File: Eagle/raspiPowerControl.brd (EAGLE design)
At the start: 100 x 80 mm, 14 parts, among them IC1 MCP1702/3 3.3, Q1 FDN360P, T1 BC847

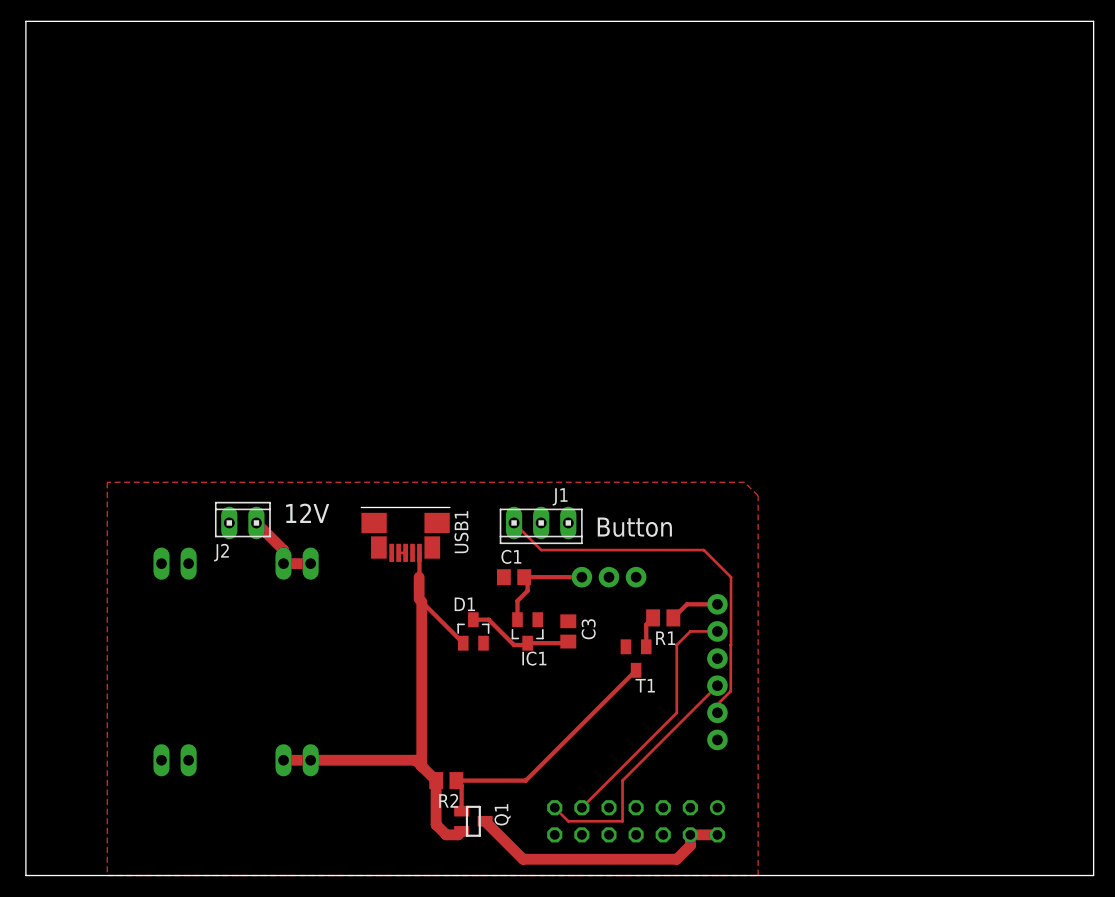
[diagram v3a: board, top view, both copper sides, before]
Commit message: Modified layout
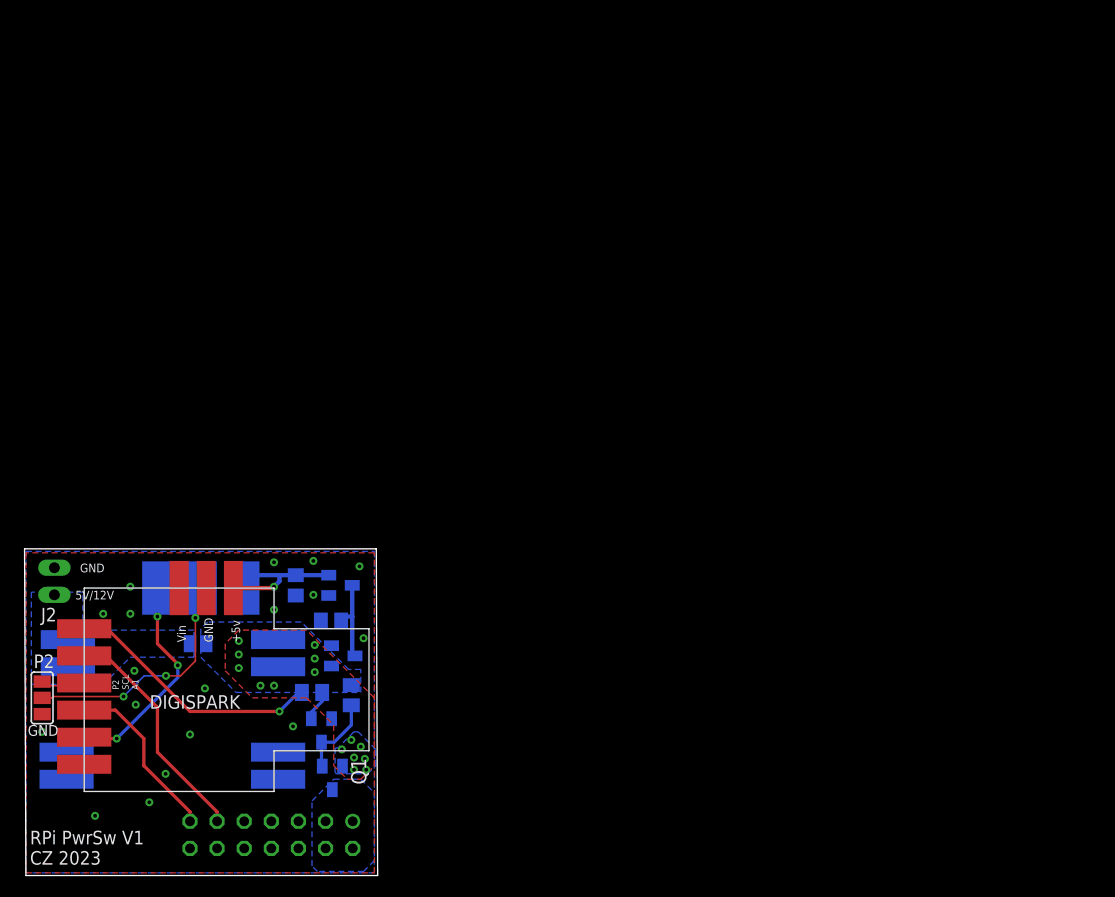
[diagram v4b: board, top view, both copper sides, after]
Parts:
- removed ATTINY85: DIGISPARK, raspiPowerControl:DIGISPARK
- removed J1: (no value), con-amp:10X03MTA
- removed USB1: MOLEX-47346-0001, usb_con-update:MOLEX-47364-0001
- added BUT: button, con-avx:009176003
- added DIGISPARK: DIGISPARKDIGISPARK-SMD, raspiPowerControl:DIGISPARK-SMD
- added P2: (no value), jumper:SJ_2
- added PWR=5V: (no value), jumper:SJ
- C3: value 100n -> 1u
- MP1584: value DCDC-MINI -> DCDC-MINIDCDC-MINI-SMD; device raspiPowerControl:DCDC-MINI -> raspiPowerControl:DCDC-MINI-SMD
- Q1: value FDN360P -> DMP3098
- moved SV1 34.2 mm to (23.0, 3.81)
- moved R1 33.6 mm to (26.8, 17.1), flipped to the bottom
- moved T1 30.2 mm to (27.7, 13.6), flipped to the bottom
- moved C3 22.2 mm to (28.6, 23.9), flipped to the bottom, turned to 180 degrees
- moved C1 20.5 mm to (25.3, 27.2), flipped to the bottom, turned to 90 degrees
- moved J2 18.5 mm to (2.67, 27.6), flipped to the bottom, turned to 90 degrees
- moved IC1 18.1 mm to (29.5, 27.2), flipped to the bottom, turned to 90 degrees
- moved Q1 13.8 mm to (28.7, 9.14), flipped to the bottom, turned to 180 degrees
- moved D1 12.4 mm to (29.7, 20.6), flipped to the bottom, turned to 90 degrees
- moved R2 12.0 mm to (30.5, 16.9), flipped to the bottom, turned to 90 degrees
- moved MP1584 8.56 mm to (13.5, 12.3), turned to 180 degrees
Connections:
- removed net +12V: J2.1, MP1584.3, MP1584.4
- removed net N$2: USB1.3, USB1.4
- removed net N$5: ATTINY85.P0, R1.1
- removed net N$6: ATTINY85.P4, J1.1
- new net 3V3: BUT.3, C1.2, DIGISPARK.5V, IC1.2
- new net BUT2: BUT.2, P2.2
- new net BUT4: BUT.1, DIGISPARK.P4
- new net P2: DIGISPARK.P2, P2.3
- new net SWPWR: DIGISPARK.P0, R1.1
- net +5V: now also MP1584.OUT+1, MP1584.OUT+2, PWR=5V.1; no longer MP1584.5, MP1584.6, USB1.1
- net GND: now also DIGISPARK.GND, J2.1, MP1584.IN-1, MP1584.IN-2, MP1584.OUT-1, MP1584.OUT-2, P2.1; no longer ATTINY85.GND, J1.2, J2.2, MP1584.1, MP1584.2, MP1584.7, MP1584.8, USB1.5
- net PWR: now also J2.2, MP1584.IN+1, MP1584.IN+2, PWR=5V.2; no longer ATTINY85.5V, C1.2, IC1.2, J1.3
- net RPDWN: now also DIGISPARK.P3; no longer ATTINY85.P3
- net SHUTDWN: now also DIGISPARK.P1; no longer ATTINY85.P1
- net VIN: now also DIGISPARK.VIN; no longer ATTINY85.VIN
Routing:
- net +5V: track 47.7 -> 0.00 mm, vias 0 -> 15
- net N$6: track 35.7 -> 0.00 mm
- net RP5V: track 24.8 -> 0.00 mm
- net SWPWR: track 0.00 -> 24.5 mm, vias 0 -> 1
- net BUT2: track 0.00 -> 22.9 mm, vias 0 -> 3
- net BUT4: track 0.00 -> 20.5 mm, vias 0 -> 3
- net N$3: track 24.2 -> 7.58 mm
- net 3V3: track 0.00 -> 14.1 mm, vias 0 -> 1
- net PWR: track 9.91 -> 0.00 mm
- net +12V: track 7.40 -> 0.00 mm
- net RPDWN: track 23.3 -> 16.2 mm
- net N$5: track 4.66 -> 0.00 mm
- net P2: track 0.00 -> 3.84 mm
- net N$1: track 10.0 -> 7.91 mm
- net SHUTDWN: track 23.3 -> 21.8 mm
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- added copper zone on layer 1, net +5V
- added copper zone on layer 16, net +5V
- added copper zone on layer 16, net GND
- added copper zone on layer 16, net PWR
- added copper zone on layer 16, net RP5V
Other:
- board size 100 x 80 mm -> 33.1 x 30.6 mm
- board text added: "3.3V"
- board text added: "5V/12V"
- board text added: "GND"
- board text added: "P2/GND"
- board text added: "P4"
- board text added: "Q1"
- board text added: "RPi PwrSw V1 CZ 2023"
- board text removed: "12V"
- board text removed: "Button"

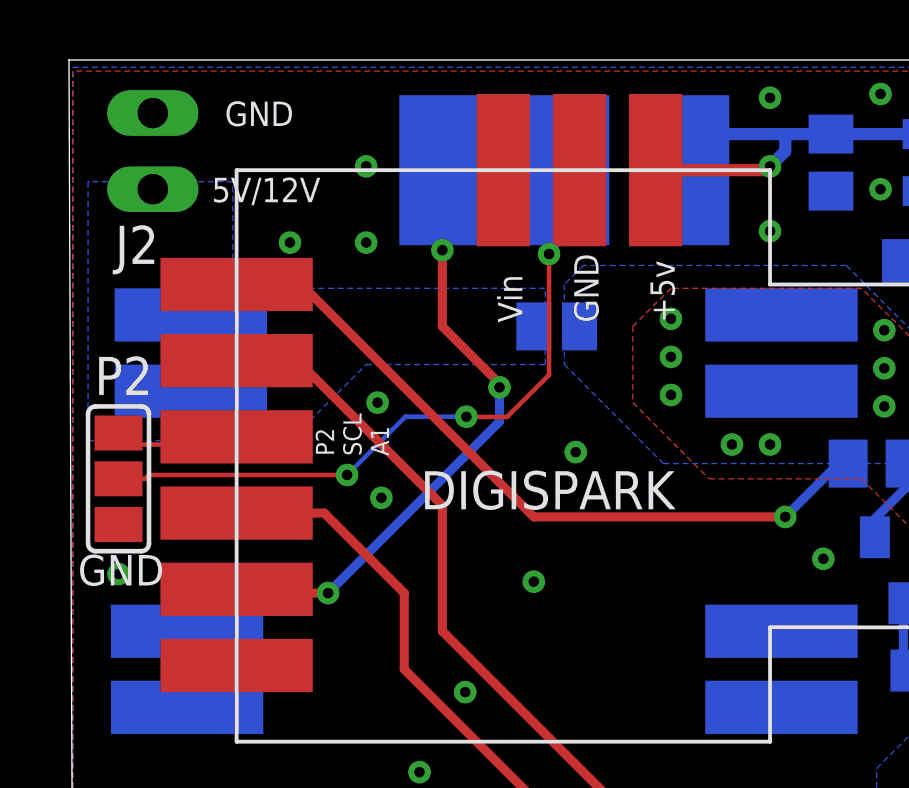
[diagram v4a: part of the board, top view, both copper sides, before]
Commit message: Smaller pads for button
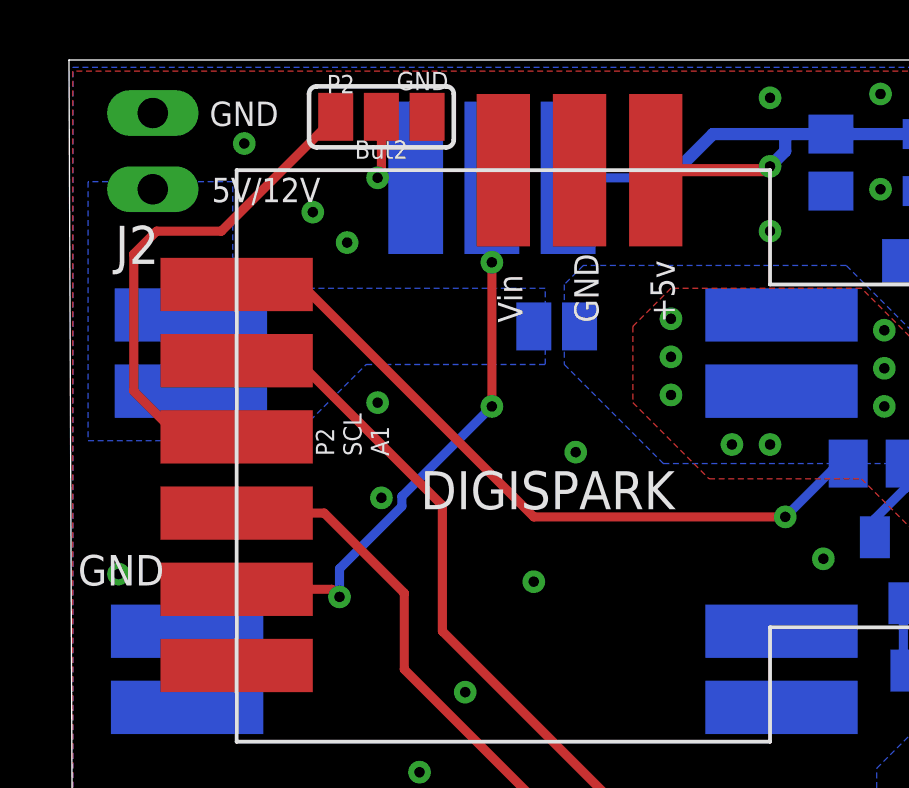
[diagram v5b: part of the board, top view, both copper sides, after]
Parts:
- removed BUT: button, con-avx:009176003
- added 3.3V, P2/GND, P4: (no value), wirepad:5-1,8
- Q1: value DMP3098 -> FDN360P
- moved P2 14.9 mm to (10.3, 28.7), turned to 180 degrees
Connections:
- net 3V3: now also 3.3V.1; no longer BUT.3
- net BUT2: now also P2/GND.1; no longer BUT.2
- net BUT4: now also P4.1; no longer BUT.1
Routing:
- net BUT2: track 22.9 -> 3.35 mm, vias 3 -> 1
- net P2: track 3.84 -> 17.4 mm
- net 3V3: track 14.1 -> 17.6 mm
- net BUT4: track 20.5 -> 19.6 mm
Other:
- board text added: "But2"
- board text removed: "3.3V"
- board text removed: "P2/GND"
- board text removed: "P4"
